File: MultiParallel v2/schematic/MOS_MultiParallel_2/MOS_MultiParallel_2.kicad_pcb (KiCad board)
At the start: 2 copper layers, 100 x 100 mm, 65 parts, among them J1 BUS, J10 ., J11 ., J12 Conn_01x01, J13 ., J14 ., J15 ., J16 ., J17 Conn_01x01, J18 Conn_01x01, J2 BUS, J20 Conn_01x12, J21 Conn_01x12, J25 ., J26 .Conn_01x01, J27 ., J28 ., J29 ., J3 BUS, J30 ., J31 Conn_02x22_Odd_Even, J4 BUS, J5 ., J6 ., J7 ., J8 ., J9 Conn_01x01, U1 SN74LVCC4245ANSR, U11 W65C22NxP, U2 74HC14, U3 6532, U4 W65C22NxP, U5 IS63WV1288DBLL-10xLI, U6 74LVC253, U7 74LVC595, U8 74AHC1G14, U9 74AHC1G08

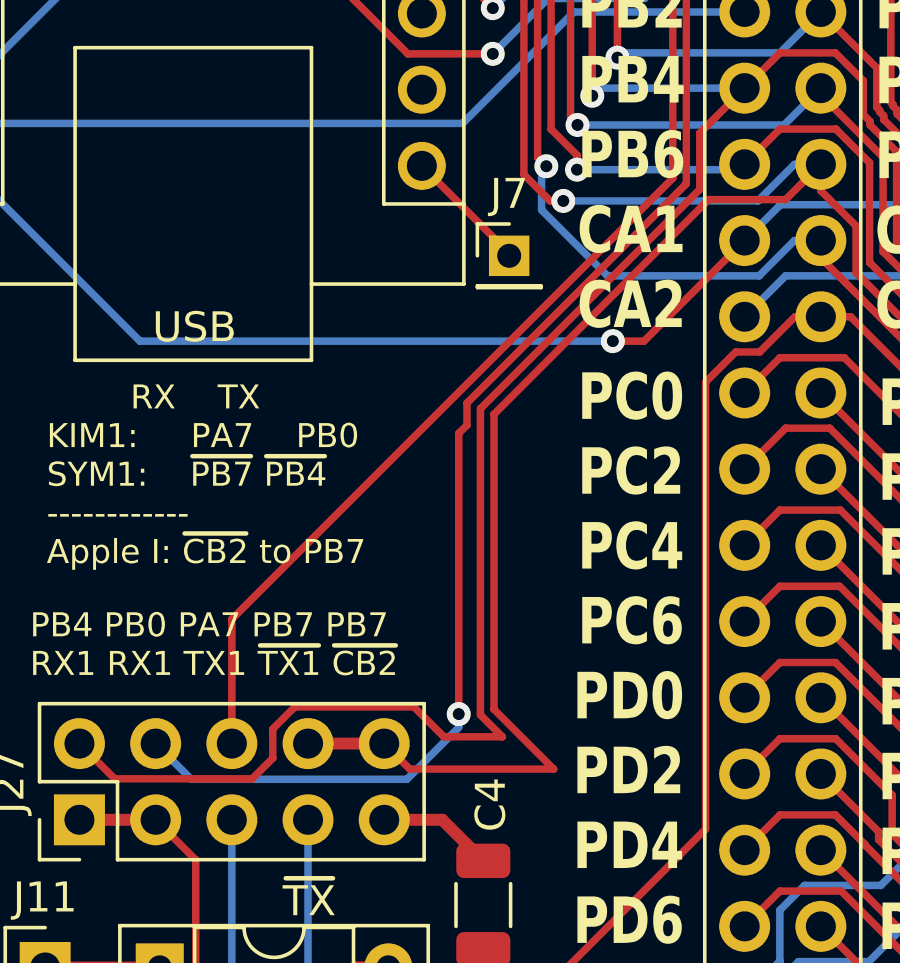
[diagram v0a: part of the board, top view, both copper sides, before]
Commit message: Apple I works, more Python work, uploadscripts for software done
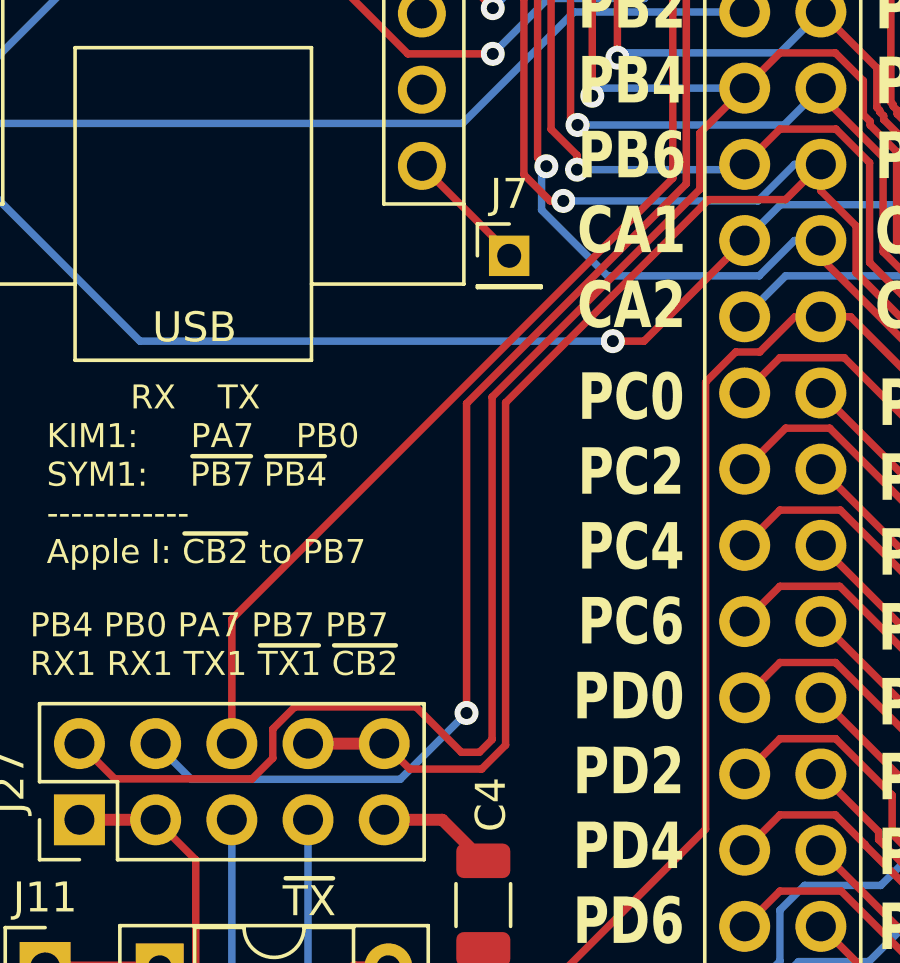
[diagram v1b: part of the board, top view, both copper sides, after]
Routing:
- net /PB7: track 125.3 -> 122.3 mm

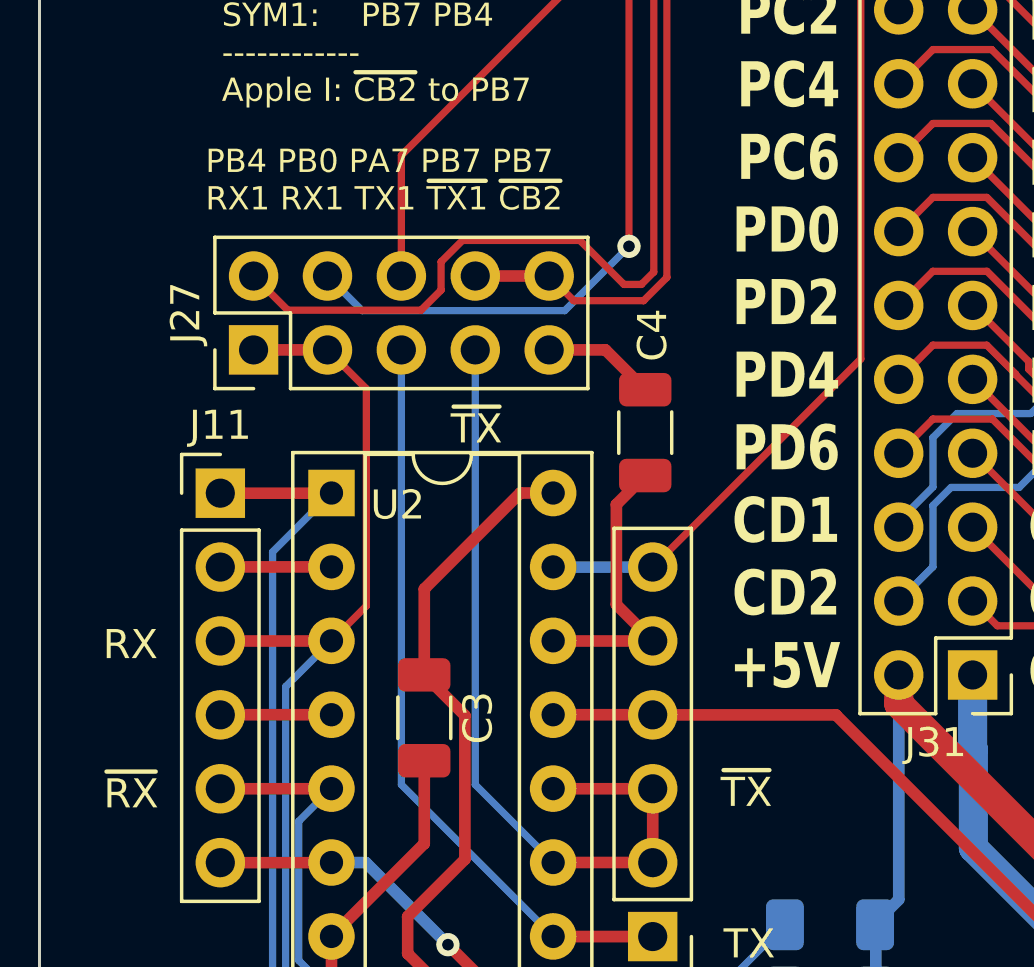
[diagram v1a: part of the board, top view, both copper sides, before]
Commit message: SYM1 & KIM1 work, RAM Board update
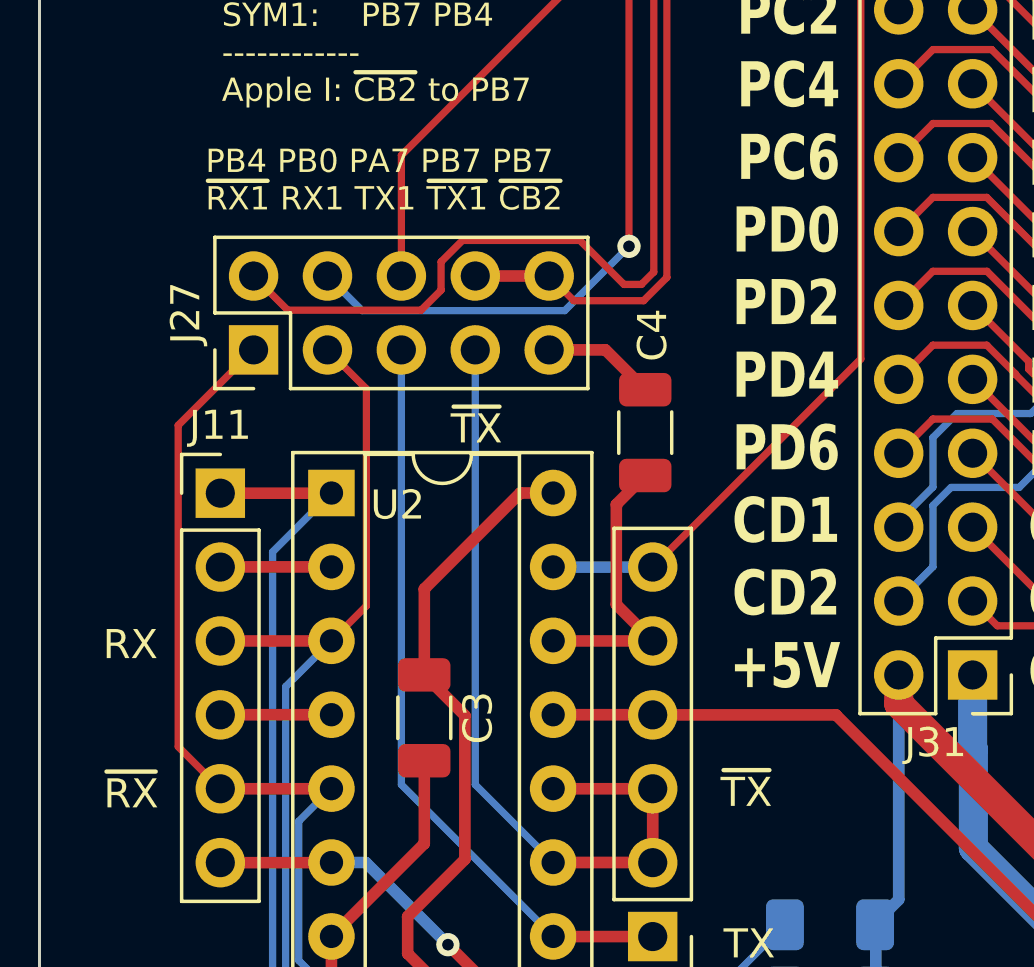
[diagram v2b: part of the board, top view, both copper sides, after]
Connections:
- J27 pad 1: /RX1# -> /~{RX1}'
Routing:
- net /~{RX1}': track 28.0 -> 44.7 mm
- net /RX1#: track 46.9 -> 44.3 mm
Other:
- board text added: "PB4 PB0 PA7 PB7 PB7 ~{RX1} RX1 TX1 ~{TX1} ~{CB2}"
- board text removed: "PB4 PB0 PA7 PB7 PB7 RX1 RX1 TX1 ~{TX1} ~{CB2}"
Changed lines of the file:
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@@
       (stroke (width 0.1) (type solid)) (layer "F.Fab"))
     (pad "1" thru_hole rect (at 0 0 90) (size 1.7 1.7) (drill 1) (layers "*.Cu" "*.Mask")
-      (net 156 "/RX1#") (pinfunction "Pin_1") (pintype "passive"))
+      (net 163 "/~{RX1}'") (pinfunction "Pin_1") (pintype "passive"))
     (pad "2" thru_hole oval (at 2.54 0 90) (size 1.7 1.7) (drill 1) (layers "*.Cu" "*.Mask")
       (net 90 "/PB4") (pinfunction "Pin_2") (pintype "passive"))
@@
     (effects (font (size 1.55 1.2) (thickness 0.2) bold) (justify left))
   )
-  (gr_text "PB4 PB0 PA7 PB7 PB7\nRX1 RX1 TX1 ~{TX1} ~{CB2}" (at 103.0478 110.3097) (layer "F.SilkS")
+  (gr_text "PB4 PB0 PA7 PB7 PB7\n~{RX1} RX1 TX1 ~{TX1} ~{CB2}" (at 103.0478 110.3097) (layer "F.SilkS")
     (effects (font (size 0.8 0.8) (thickness 0.15)) (justify left bottom))
   )
@@
   (segment (start 134.463 77.9226) (end 134.463 93.722093) (width 0.25) (layer "B.Cu") (net 153))
   (segment (start 107.3758 127.5792) (end 103.5608 127.5792) (width 0.4) (layer "F.Cu") (net 154))
-  (segment (start 107.2388 115.040331) (end 104.6988 115.040331) (width 0.4) (layer "F.Cu") (net 156))
   (segment (start 103.5558 125.0442) (end 107.3708 125.0442) (width 0.4) (layer "F.Cu") (net 156))
   (segment (start 108.5758 116.377331) (end 108.5758 123.8392) (width 0.25) (layer "F.Cu") (net 156))
@@
   (segment (start 119.5832 70.3834) (end 116.1134 70.3834) (width 0.25) (layer "F.Cu") (net 161))
   (segment (start 119.5832 67.8434) (end 116.1134 67.8434) (width 0.25) (layer "F.Cu") (net 162))
+  (segment (start 104.6988 115.040331) (end 102.108 117.631131) (width 0.25) (layer "F.Cu") (net 163))
+  (segment (start 102.108 117.631131) (end 102.108 128.6764) (width 0.25) (layer "F.Cu") (net 163))
+  (segment (start 102.108 128.6764) (end 103.5558 130.1242) (width 0.25) (layer "F.Cu") (net 163))
   (segment (start 103.5558 130.1242) (end 107.3708 130.1242) (width 0.4) (layer "F.Cu") (net 163))
   (segment (start 121.031 136.7282) (end 106.9528 136.7282) (width 0.25) (layer "B.Cu") (net 163))

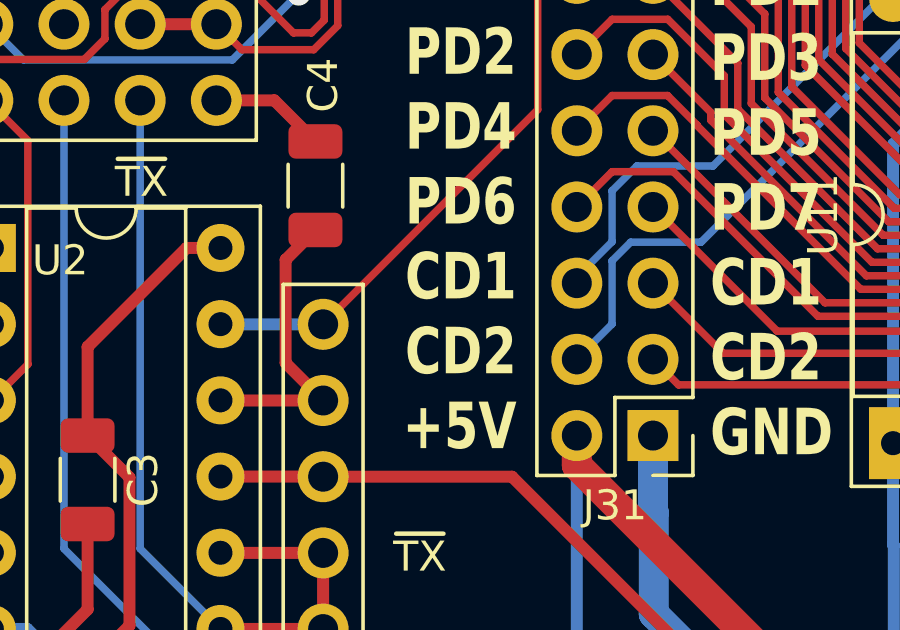
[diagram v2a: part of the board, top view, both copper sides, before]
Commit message: DREAM6800 working with glitches
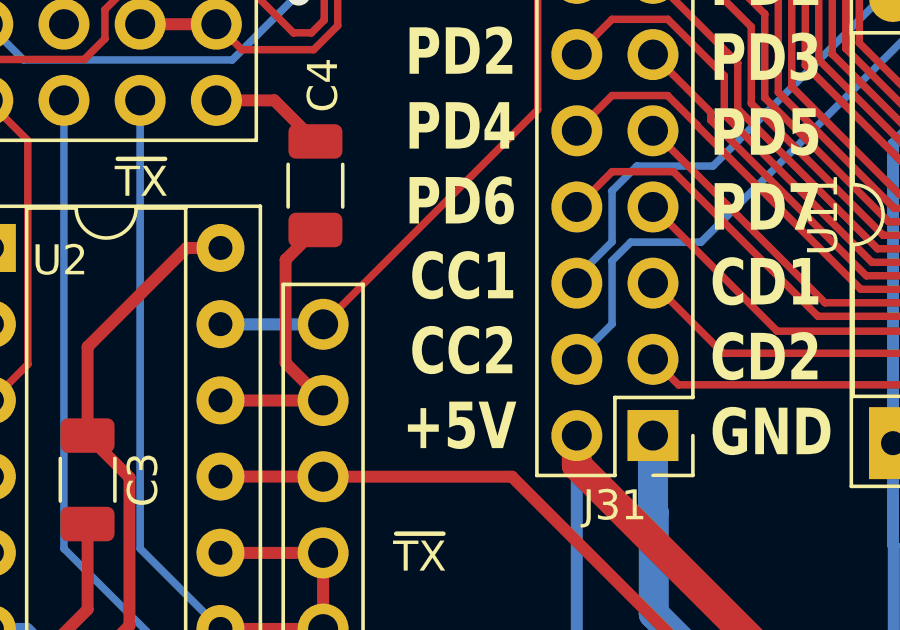
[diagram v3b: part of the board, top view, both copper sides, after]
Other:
- board text added: "PC0 PC2 PC4 PC6 PD0 PD2 PD4 PD6 CC1 CC2 +5V"
- board text removed: "PC0 PC2 PC4 PC6 PD0 PD2 PD4 PD6 CD1 CD2 +5V"
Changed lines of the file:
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@@
     (effects (font (size 1.55 1.2) (thickness 0.2) bold) (justify right))
   )
-  (gr_text "PC0\nPC2\nPC4\nPC6\nPD0\nPD2\nPD4\nPD6\nCD1\nCD2\n+5V" (at 124.8664 113.4364) (layer "F.SilkS")
+  (gr_text "PC0\nPC2\nPC4\nPC6\nPD0\nPD2\nPD4\nPD6\nCC1\nCC2\n+5V" (at 124.8664 113.4364) (layer "F.SilkS")
     (effects (font (size 1.55 1.2) (thickness 0.2) bold) (justify right))
   )
